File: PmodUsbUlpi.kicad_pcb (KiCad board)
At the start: 2 copper layers, 25 x 40 mm, 22 parts, among them J1 USB_C_Receptacle_USB2.0, J2 PMOD1, J3 PMOD2, U1 TPS76318, U2 USB3320

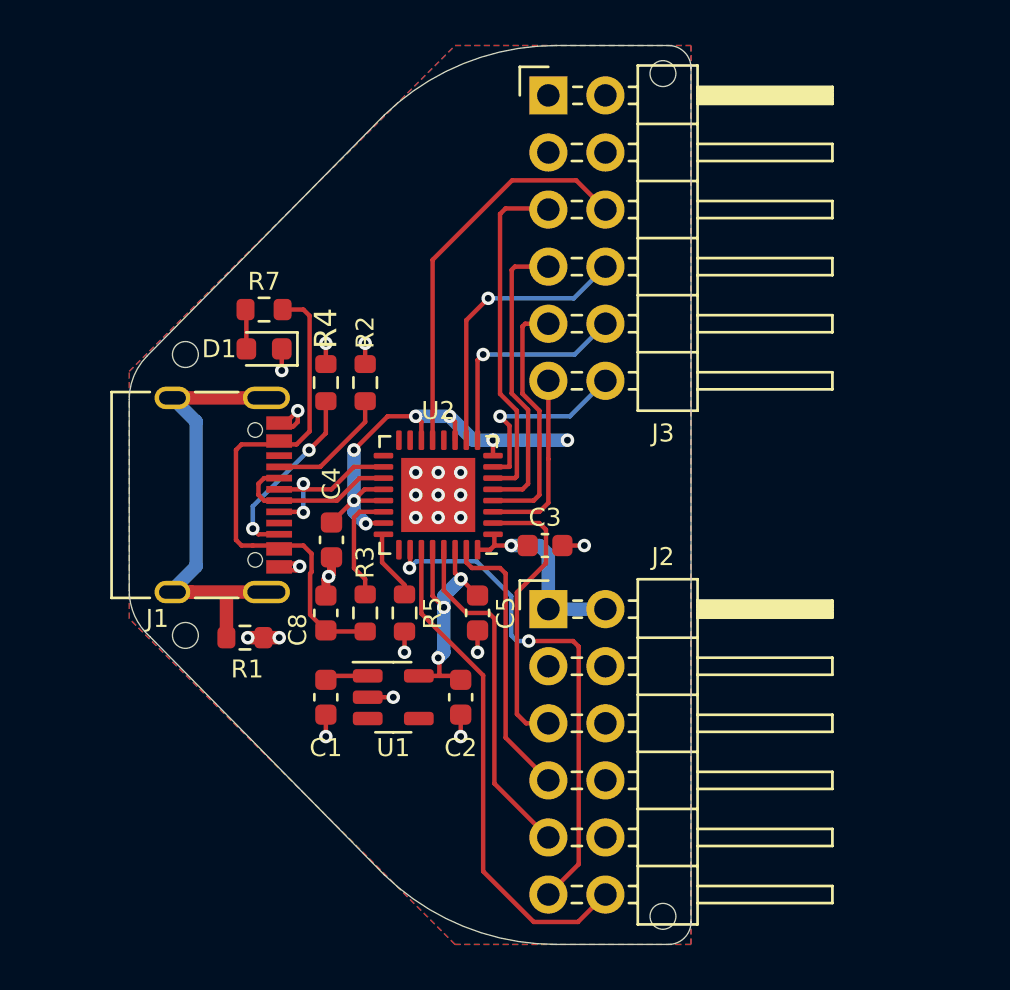
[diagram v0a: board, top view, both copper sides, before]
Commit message: First Version with Waveshare Pinout
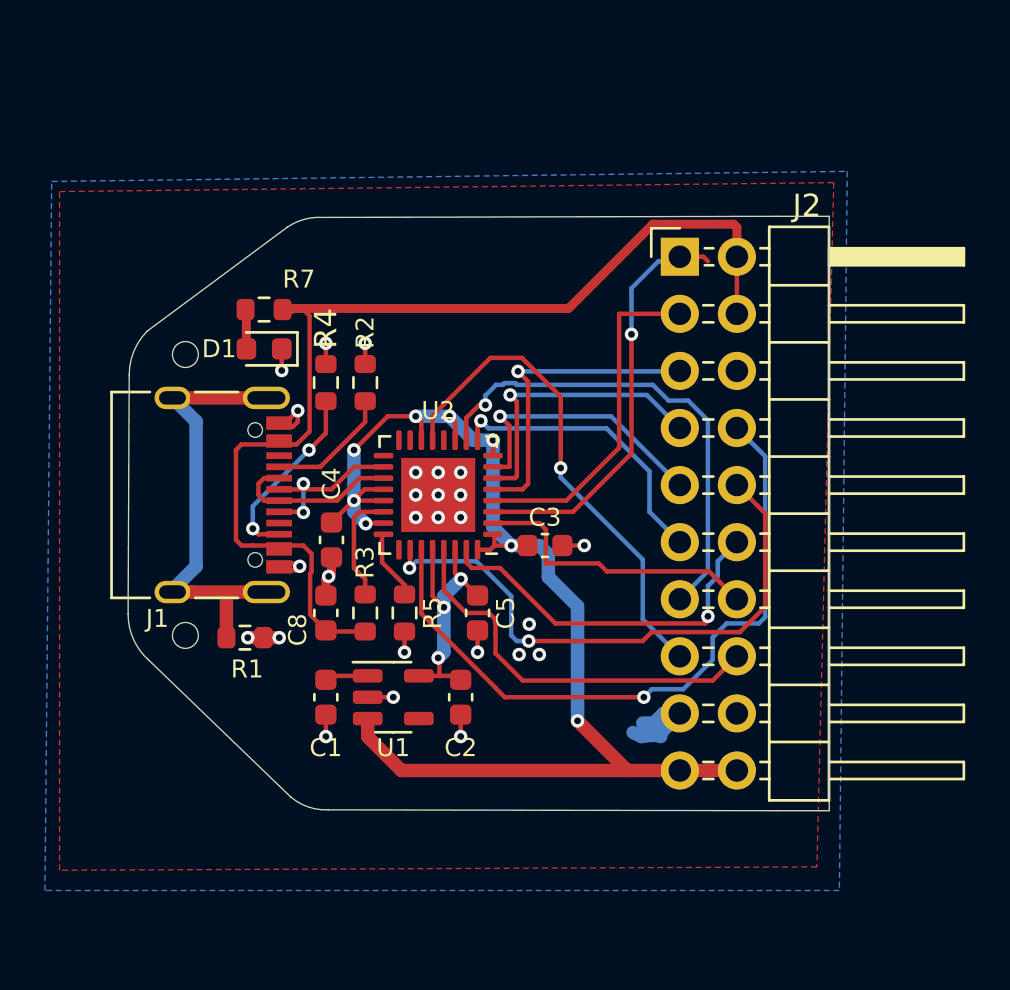
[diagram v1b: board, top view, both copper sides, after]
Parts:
- removed J3: PMOD2, Connector_PinHeader_2.54mm:PinHeader_2x06_P2.54mm_Horizontal
- removed the REF** at (161.2, 118.8)
- removed the REF** at (161.2, 81.2)
- added REFm**: KiCad-Logo2_5mm_SilkScreen, Symbol:KiCad-Logo2_5mm_SilkScreen, B.Cu at (154.0, 101.0)
- J2: value PMOD1 -> 2x10 Header; footprint Connector_PinHeader_2.54mm:PinHeader_2x06_P2.54mm_Horizontal -> Connector_PinHeader_2.54mm:PinHeader_2x10_P2.54mm_Horizontal
- moved J2 16.7 mm to (162.0, 89.4)
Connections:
- J2 pad 1: +3V3 -> /DATA0
- J2 pad 10: Net-(J2-Pad10) -> /CLK
- J2 pad 11: /CLK -> /DATA5
- J2 pad 12: /RESET -> /DIR
- J2 pad 2: +3V3 -> VBUS
- J2 pad 3: GND -> /DATA1
- J2 pad 4: GND -> VBUS
- J2 pad 5: /NXT -> /DATA2
- J2 pad 7: /DIR -> /DATA3
- J2 pad 8: Net-(J2-Pad8) -> /RESET
- J2 pad 9: /STP -> /DATA4
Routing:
- net VBUS: track 23.8 -> 65.2 mm
- net +3V3: track 33.7 -> 59.4 mm
- net /DATA0: track 8.06 -> 18.7 mm, vias 0 -> 1
- net /DATA6: track 12.5 -> 21.9 mm
- net /RESET: track 22.3 -> 30.7 mm, vias 0 -> 1
- net GND: track 16.9 -> 22.7 mm, vias 23 -> 26
- net /DATA7: track 17.7 -> 22.3 mm, vias 0 -> 1
- net /DATA1: track 11.2 -> 15.4 mm
- net /DIR: track 12.5 -> 16.5 mm, vias 0 -> 1
- net /DATA4: track 8.51 -> 12.4 mm
- net /CLK: track 22.7 -> 25.9 mm
- net /DATA5: track 9.92 -> 13.1 mm
- net /STP: track 15.3 -> 17.8 mm
- net /DATA3: track 15.4 -> 13.1 mm, vias 0 -> 1
- net /DATA2: track 13.2 -> 14.1 mm, vias 0 -> 1
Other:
- board size 25 x 40 mm -> 31.2 x 26.5 mm
- net class Default removed
- board text added: "5V"
- board text added: "NC"
- board text added: "USB ULPI Module Tobias Müller, twam.info New Pinout, 2021-05-18 by Hans Baier"
- board text removed: "USB PMOD ULPI Rev. 2, 2021-02-26 Tobias Müller, twam.info"

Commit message: first version with 1.8V
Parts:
- moved REFm** 10.0 mm to (152.0, 91.2), turned to 180 degrees
- moved C3 1.70 mm to (155.2, 103.8), turned to -90 degrees
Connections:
- C3 pad 1: +3V3 -> +1V8
- J2 pad 6: Net-(J2-Pad6) -> unconnected-(J2-Pad6)
- U1 pad 4: Net-(U1-Pad4) -> unconnected-(U1-Pad4)
- U2 pad 1: +3V3 -> +1V8
- U2 pad 11: +3V3 -> +1V8
- U2 pad 12: Net-(U2-Pad12) -> unconnected-(U2-Pad12)
- U2 pad 14: +3V3 -> +1V8
- U2 pad 15: Net-(U2-Pad15) -> unconnected-(U2-Pad15)
- U2 pad 16: Net-(U2-Pad16) -> unconnected-(U2-Pad16)
- U2 pad 17: Net-(U2-Pad17) -> unconnected-(U2-Pad17)
- U2 pad 25: Net-(U2-Pad25) -> unconnected-(U2-Pad25)
- U2 pad 32: +3V3 -> +1V8
- U2 pad 8: +3V3 -> +1V8
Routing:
- net +1V8: track 11.9 -> 34.3 mm, vias 3 -> 7
- net +3V3: track 59.4 -> 39.9 mm, vias 8 -> 2
- net /CLK: track 25.9 -> 16.9 mm, vias 2 -> 3
- net /DATA6: track 21.9 -> 17.3 mm
- net /DATA3: track 13.1 -> 9.24 mm
- net /DATA4: track 12.4 -> 9.11 mm, vias 1 -> 0
- net /DATA5: track 13.1 -> 16.0 mm, vias 1 -> 0
- net /DIR: track 16.5 -> 13.7 mm, vias 1 -> 2
- net GND: track 22.7 -> 24.5 mm, vias 26 -> 23
- net /DATA0: track 18.7 -> 16.9 mm
- net /RESET: track 30.7 -> 32.3 mm, vias 1 -> 0
- net /DATA2: track 14.1 -> 12.5 mm
- net /DATA1: track 15.4 -> 14.2 mm, vias 0 -> 1
- net /STP: track 17.8 -> 17.0 mm
- net /DATA7: track 22.3 -> 21.7 mm
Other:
- board text added: "USB ULPI Module Tobias Müller, twam.info New Pinout/1.8V Version by Hans Baier"
- board text removed: "JLCJLCJLCJLC"
- board text removed: "USB ULPI Module Tobias Müller, twam.info New Pinout, 2021-05-18 by Hans Baier"

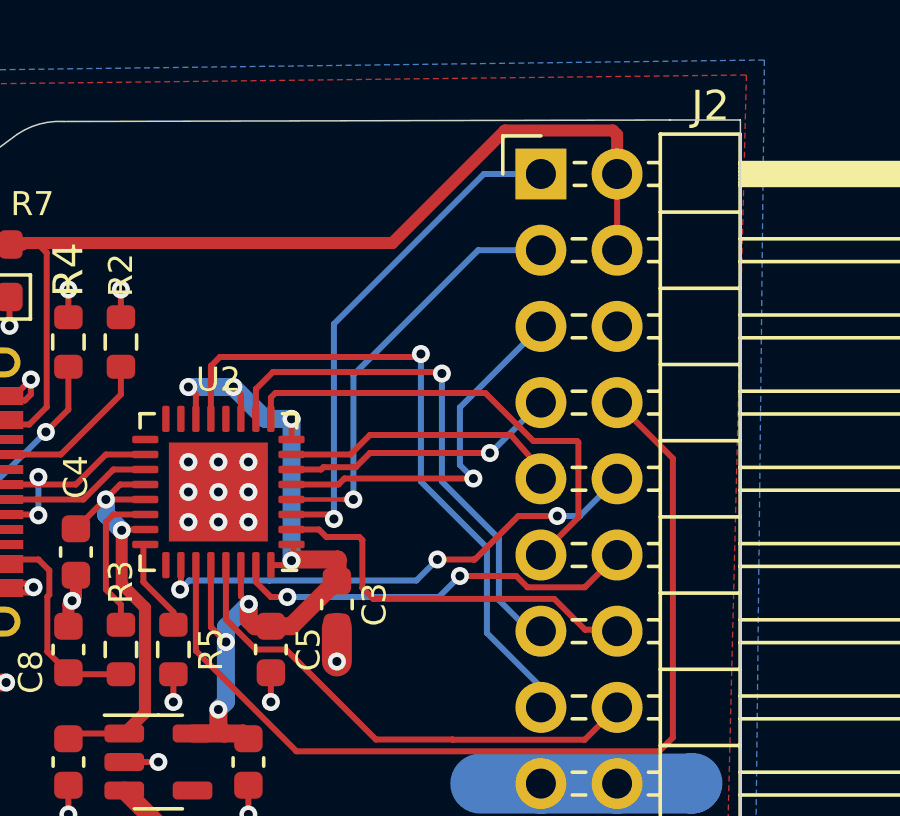
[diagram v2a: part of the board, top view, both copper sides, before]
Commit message: Tweak a couple of traces (better crossings)
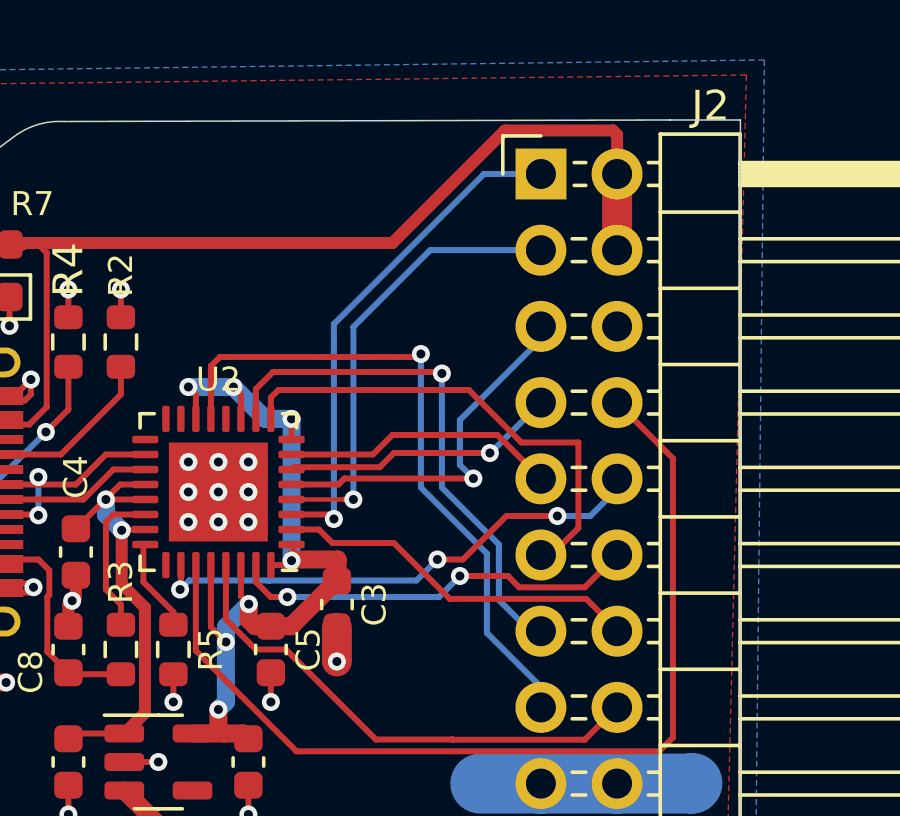
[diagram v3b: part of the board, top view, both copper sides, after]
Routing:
- net /NXT: track 13.2 -> 12.2 mm
- net /DATA1: track 14.2 -> 15.1 mm
